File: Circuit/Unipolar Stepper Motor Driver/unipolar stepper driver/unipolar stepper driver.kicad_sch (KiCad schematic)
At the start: 20 parts, among them Q1 S8050, Q2 S8050, Q3 S8050, Q4 S8050

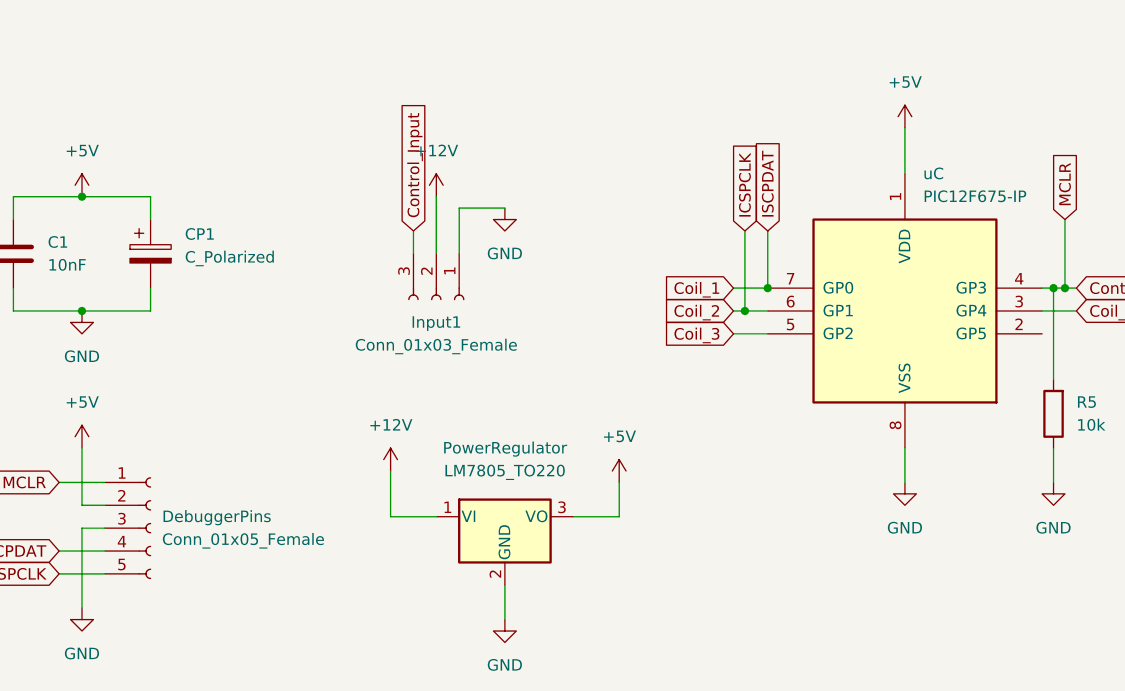
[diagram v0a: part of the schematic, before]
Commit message: Modified unipolar driver circuit and generated outputs
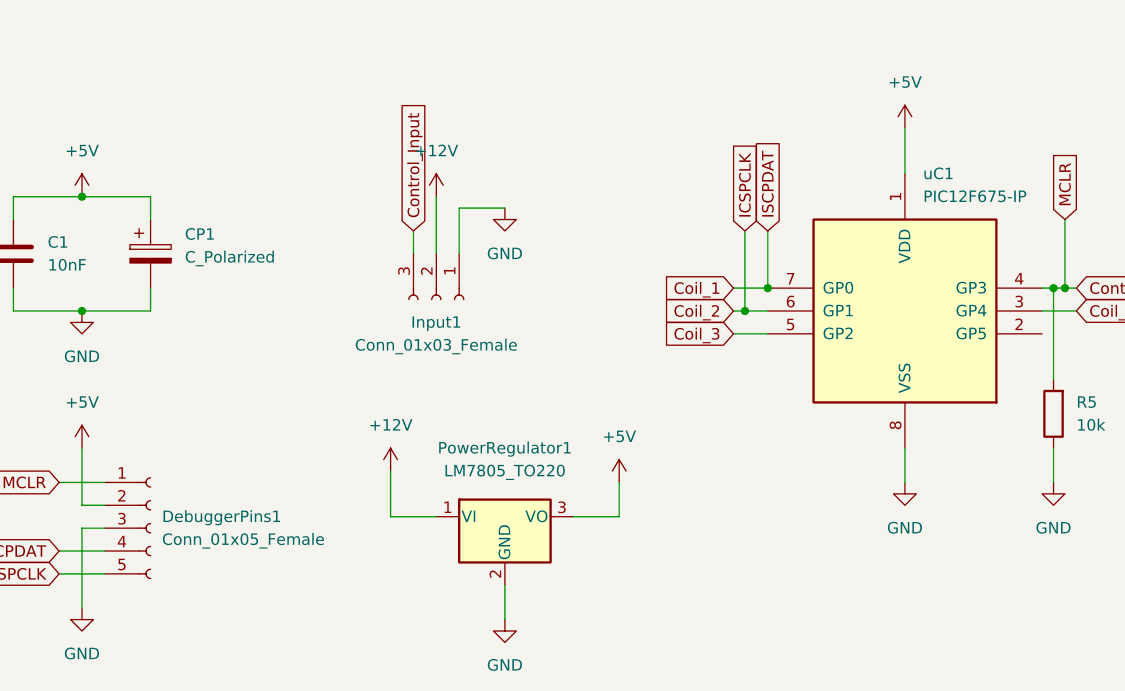
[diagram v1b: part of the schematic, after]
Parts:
- renumbered DebuggerPins to DebuggerPins1, PowerRegulator to PowerRegulator1, uC to uC1
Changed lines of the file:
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@@
   (symbol (lib_id "Connector:Conn_01x05_Female") (at 57.15 120.65 0) (unit 1)
     (in_bom yes) (on_board yes) (fields_autoplaced)
-    (property "Reference" "DebuggerPins" (id 0) (at 58.42 119.3799 0)
+    (property "Reference" "DebuggerPins1" (id 0) (at 58.42 119.3799 0)
       (effects (font (size 1.27 1.27)) (justify left))
     )
@@
   (symbol (lib_id "power:+12V") (at 83.82 114.3 0) (unit 1)
     (in_bom yes) (on_board yes) (fields_autoplaced)
-    (property "Reference" "#PWR?" (id 0) (at 83.82 118.11 0)
+    (property "Reference" "#PWR0107" (id 0) (at 83.82 118.11 0)
       (effects (font (size 1.27 1.27)) hide)
     )
@@
   (symbol (lib_id "Regulator_Linear:LM7805_TO220") (at 96.52 119.38 0) (unit 1)
     (in_bom yes) (on_board yes) (fields_autoplaced)
-    (property "Reference" "PowerRegulator" (id 0) (at 96.52 111.76 0))
+    (property "Reference" "PowerRegulator1" (id 0) (at 96.52 111.76 0))
     (property "Value" "LM7805_TO220" (id 1) (at 96.52 114.3 0))
     (property "Footprint" "Package_TO_SOT_THT:TO-220-3_Vertical" (id 2) (at 96.52 113.665 0)
@@
   (symbol (lib_id "power:+5V") (at 49.53 111.76 0) (unit 1)
     (in_bom yes) (on_board yes) (fields_autoplaced)
-    (property "Reference" "#PWR?" (id 0) (at 49.53 115.57 0)
+    (property "Reference" "#PWR0114" (id 0) (at 49.53 115.57 0)
       (effects (font (size 1.27 1.27)) hide)
     )
@@
   (symbol (lib_id "MCU_Microchip_PIC12:PIC12F675-IP") (at 140.97 96.52 0) (unit 1)
     (in_bom yes) (on_board yes) (fields_autoplaced)
-    (property "Reference" "uC" (id 0) (at 142.9894 81.28 0)
+    (property "Reference" "uC1" (id 0) (at 142.9894 81.28 0)
       (effects (font (size 1.27 1.27)) (justify left))
     )
@@
   (symbol (lib_id "power:+12V") (at 88.9 83.82 0) (unit 1)
     (in_bom yes) (on_board yes) (fields_autoplaced)
-    (property "Reference" "#PWR?" (id 0) (at 88.9 87.63 0)
+    (property "Reference" "#PWR0111" (id 0) (at 88.9 87.63 0)
       (effects (font (size 1.27 1.27)) hide)
     )
@@
   (symbol (lib_id "power:GND") (at 49.53 129.54 0) (unit 1)
     (in_bom yes) (on_board yes) (fields_autoplaced)
-    (property "Reference" "#PWR?" (id 0) (at 49.53 135.89 0)
+    (property "Reference" "#PWR0115" (id 0) (at 49.53 135.89 0)
       (effects (font (size 1.27 1.27)) hide)
     )
@@
   (symbol (lib_id "power:+5V") (at 109.22 115.57 0) (unit 1)
     (in_bom yes) (on_board yes) (fields_autoplaced)
-    (property "Reference" "#PWR?" (id 0) (at 109.22 119.38 0)
+    (property "Reference" "#PWR0112" (id 0) (at 109.22 119.38 0)
       (effects (font (size 1.27 1.27)) hide)
     )
@@
   (symbol (lib_id "power:GND") (at 96.52 130.81 0) (unit 1)
     (in_bom yes) (on_board yes) (fields_autoplaced)
-    (property "Reference" "#PWR?" (id 0) (at 96.52 137.16 0)
+    (property "Reference" "#PWR0113" (id 0) (at 96.52 137.16 0)
       (effects (font (size 1.27 1.27)) hide)
     )
@@
       (reference "#PWR0106") (unit 1) (value "GND") (footprint "")
     )
+    (path "/2c68e754-48b7-4e80-a996-f241c915bf5e"
+      (reference "#PWR0107") (unit 1) (value "+12V") (footprint "")
+    )
     (path "/3e074500-d08a-4ad5-bc11-4dbe6fbe24ff"
       (reference "#PWR0108") (unit 1) (value "GND") (footprint "")
@@
       (reference "#PWR0110") (unit 1) (value "+5V") (footprint "")
     )
-    (path "/2c68e754-48b7-4e80-a996-f241c915bf5e"
-      (reference "#PWR?") (unit 1) (value "+12V") (footprint "")
+    (path "/ae12c49a-ea46-48de-89a0-d17f075c5a04"
+      (reference "#PWR0111") (unit 1) (value "+12V") (footprint "")
+    )
+    (path "/f011e4cb-4780-4f9e-b9d0-f1e5f067c44d"
+      (reference "#PWR0112") (unit 1) (value "+5V") (footprint "")
+    )
+    (path "/f8209c75-0a83-44fa-989f-484243aa7138"
+      (reference "#PWR0113") (unit 1) (value "GND") (footprint "")
     )
     (path "/51500517-830d-45f8-8448-0acbf43a695b"
-      (reference "#PWR?") (unit 1) (value "+5V") (footprint "")
-    )
-    (path "/ae12c49a-ea46-48de-89a0-d17f075c5a04"
-      (reference "#PWR?") (unit 1) (value "+12V") (footprint "")
+      (reference "#PWR0114") (unit 1) (value "+5V") (footprint "")
     )
     (path "/c1eb79c8-c971-4813-8f4e-4ef413e23f8e"
-      (reference "#PWR?") (unit 1) (value "GND") (footprint "")
-    )
-    (path "/f011e4cb-4780-4f9e-b9d0-f1e5f067c44d"
-      (reference "#PWR?") (unit 1) (value "+5V") (footprint "")
-    )
-    (path "/f8209c75-0a83-44fa-989f-484243aa7138"
-      (reference "#PWR?") (unit 1) (value "GND") (footprint "")
+      (reference "#PWR0115") (unit 1) (value "GND") (footprint "")
     )
     (path "/7c3df708-fb44-40cc-b435-cd67e8cec48a"
@@
     )
     (path "/1e4b633a-1e18-472b-b95a-3c8b9a6871c1"
-      (reference "DebuggerPins") (unit 1) (value "Conn_01x05_Female") (footprint "Connector_PinHeader_2.54mm:PinHeader_1x05_P2.54mm_Vertical")
+      (reference "DebuggerPins1") (unit 1) (value "Conn_01x05_Female") (footprint "Connector_PinHeader_2.54mm:PinHeader_1x05_P2.54mm_Vertical")
     )
     (path "/c7872803-5b3e-4e37-94ac-c4dc2bc4adfb"
@@
     )
     (path "/2e1023b4-e8f1-4a23-af54-5e7547aa39be"
-      (reference "PowerRegulator") (unit 1) (value "LM7805_TO220") (footprint "Package_TO_SOT_THT:TO-220-3_Vertical")
+      (reference "PowerRegulator1") (unit 1) (value "LM7805_TO220") (footprint "Package_TO_SOT_THT:TO-220-3_Vertical")
     )
     (path "/59fc765e-1357-4c94-9529-5635418c7d73"
@@
     )
     (path "/77cfe682-cc36-4979-823b-05ea5f187ba7"
-      (reference "uC") (unit 1) (value "PIC12F675-IP") (footprint "Package_DIP:DIP-8_W7.62mm")
-    )
-  )
+      (reference "uC1") (unit 1) (value "PIC12F675-IP") (footprint "Package_DIP:DIP-8_W7.62mm")
+    )
+  )
